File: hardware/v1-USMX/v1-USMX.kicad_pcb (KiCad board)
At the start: 2 copper layers, 91.4 x 48.8 mm, 38 parts, among them IC1 MAX98357AETE+T (L), IC2 MAX98357AETE+T (R), J1 +5v_POWER, J2 Conn_01x04, J3 10118192-0002LF, J4 Serial_Breakout, U1 ESP32-S3-WROOM-1, U2 AZ1084-3.3

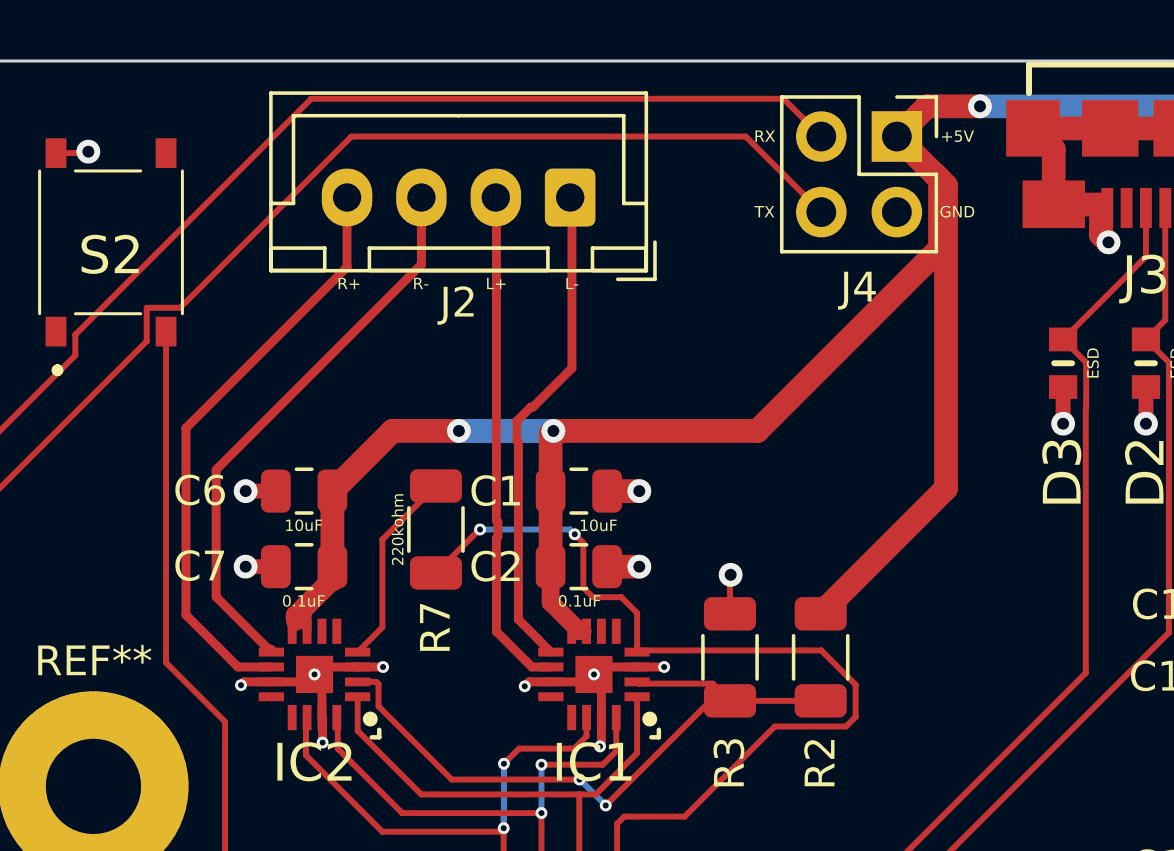
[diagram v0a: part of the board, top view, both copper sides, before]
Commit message: Increased the size of some silk screen
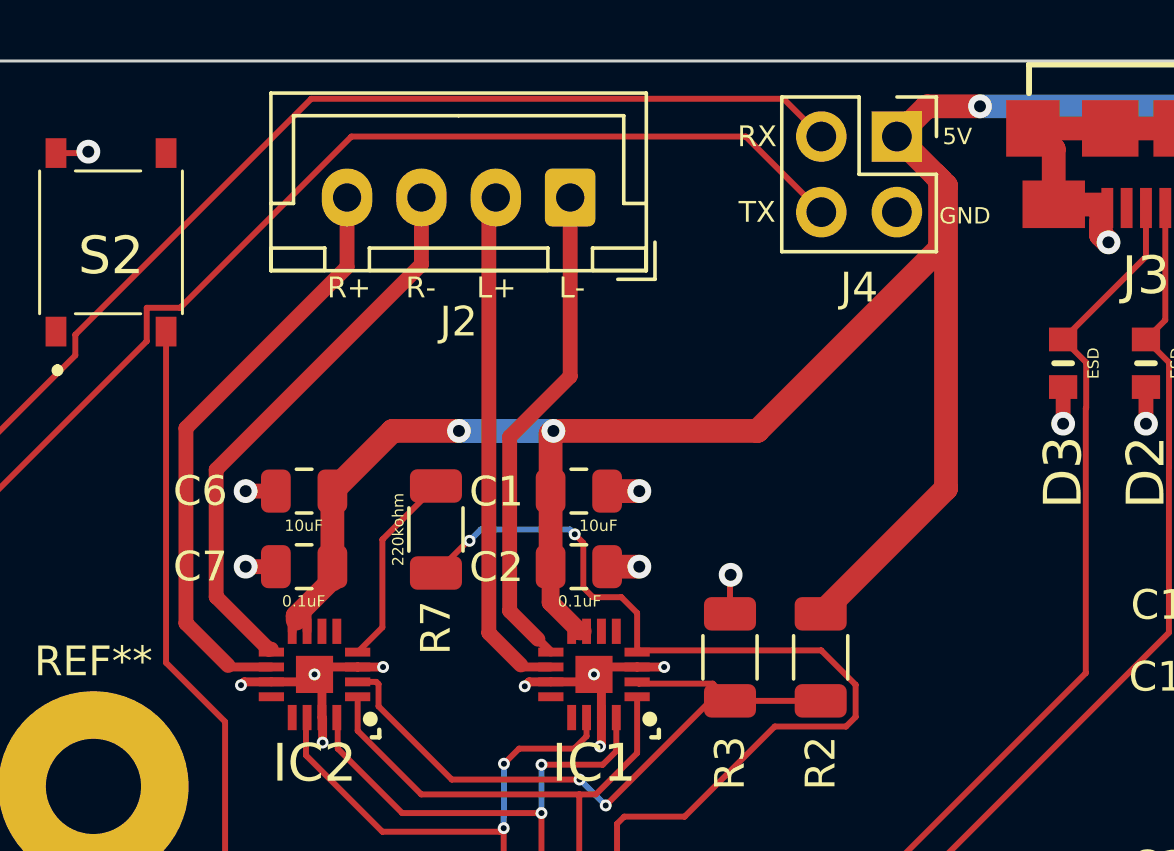
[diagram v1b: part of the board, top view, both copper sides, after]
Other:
- board text added: "5V"
- board text removed: "+5V"

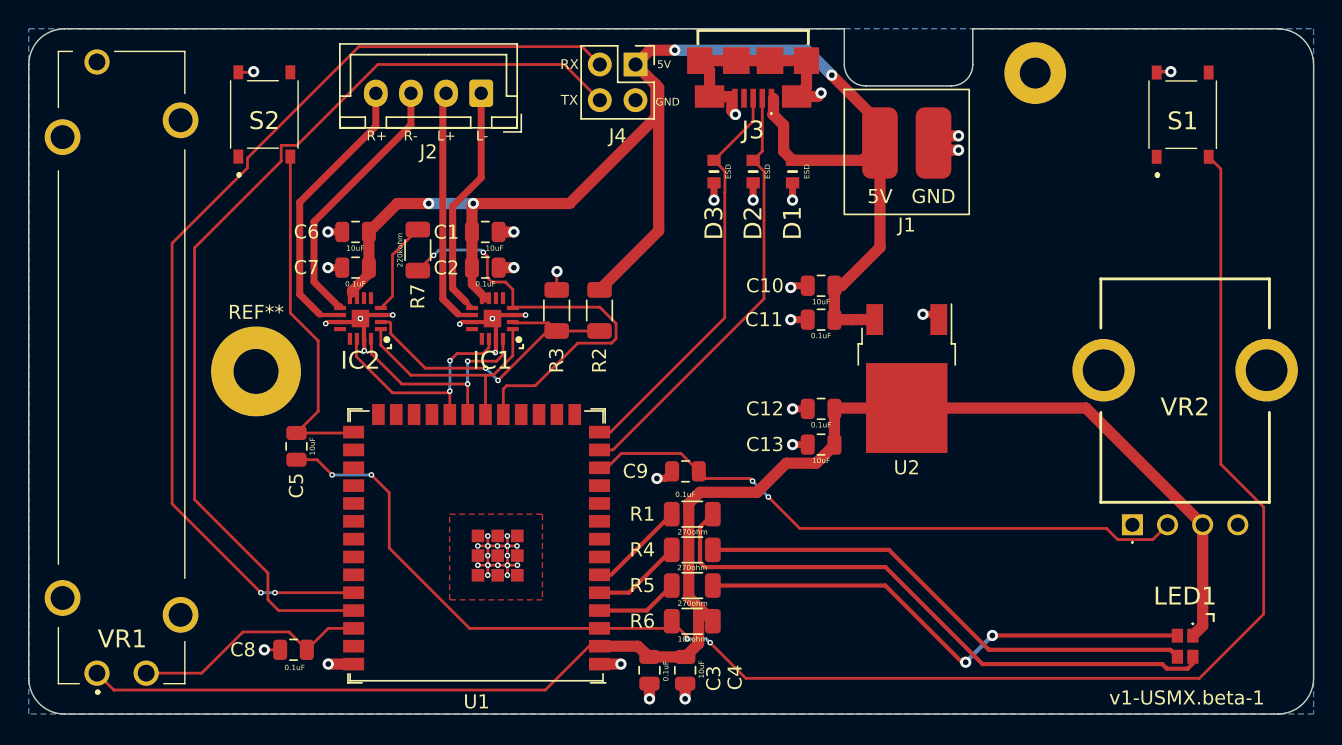
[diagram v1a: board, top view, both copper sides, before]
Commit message: Added ground plane to top, vias at extremeties
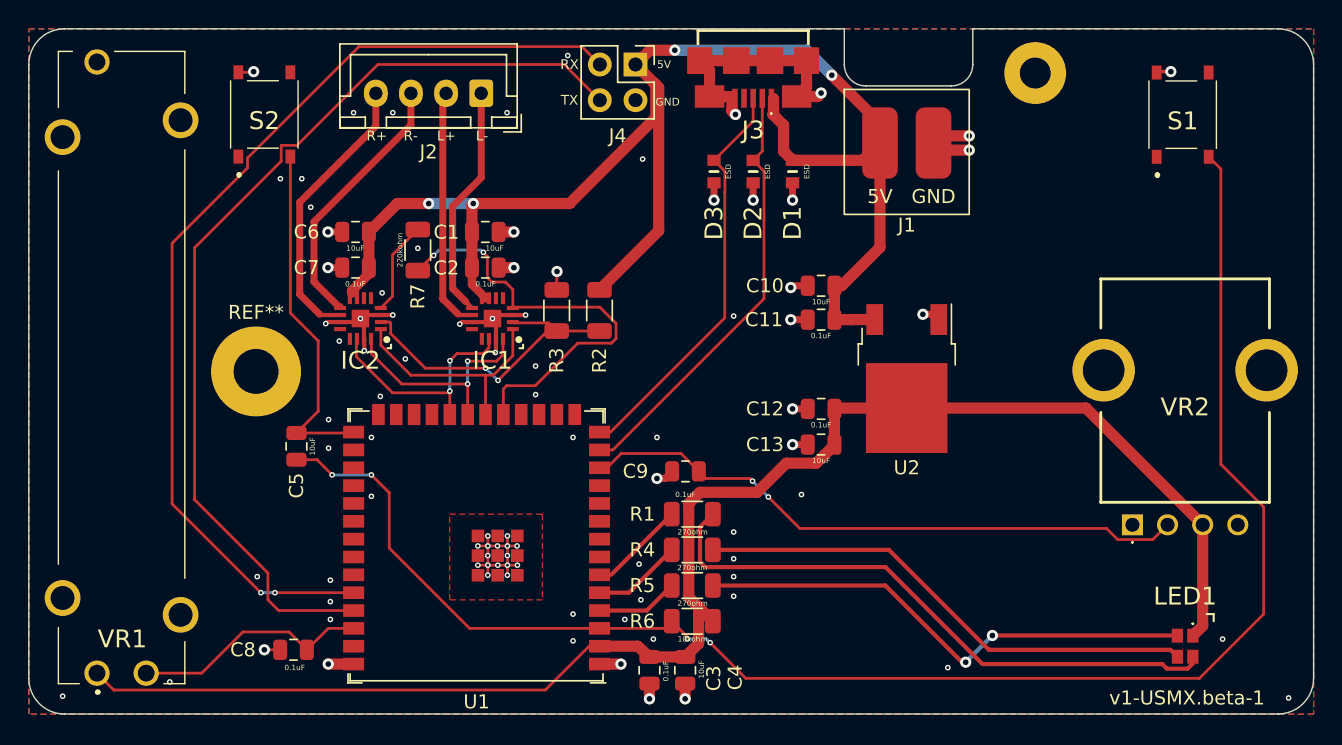
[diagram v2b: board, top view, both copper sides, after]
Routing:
- net GND: track 72.3 -> 73.9 mm, vias 49 -> 91

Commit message: Removed unused screw holes, corrected shape of pads
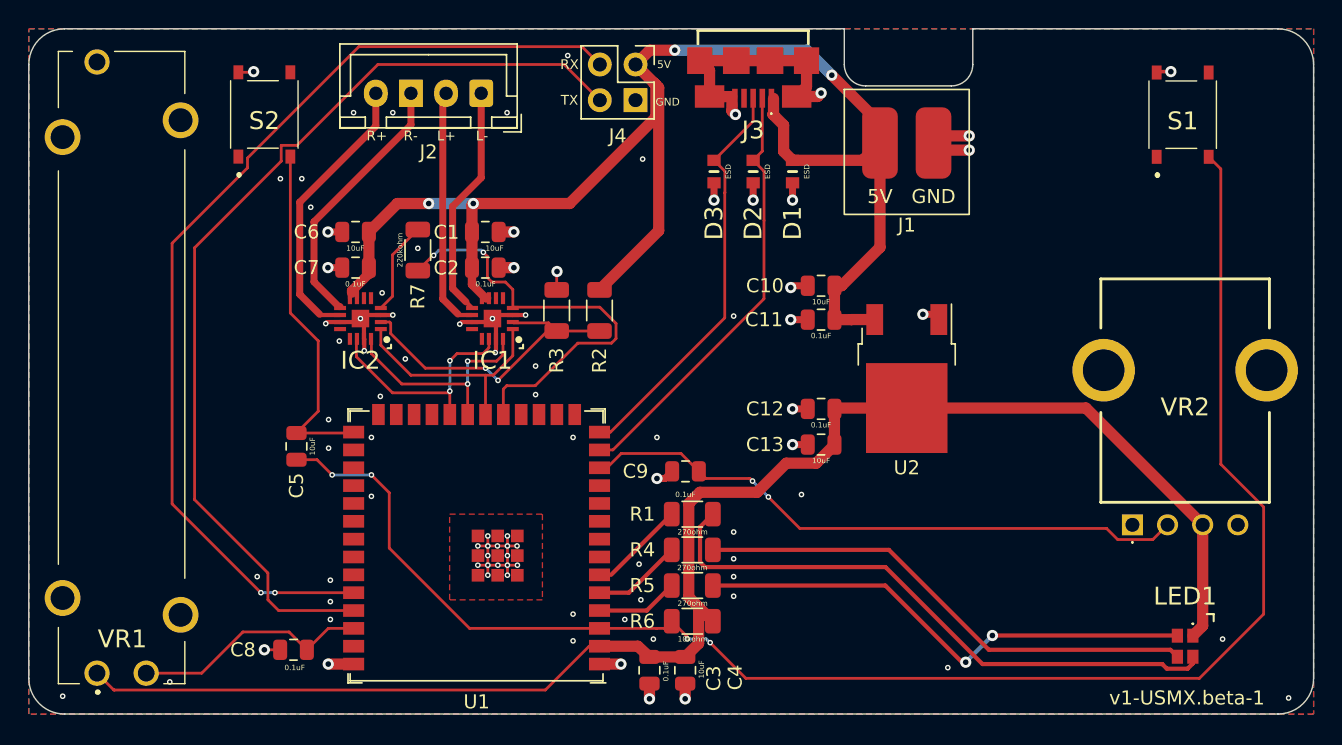
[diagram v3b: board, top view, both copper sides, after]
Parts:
- removed ?: , 
- removed REF**: MountingHole_3.2mm_M3_Pad, MountingHole:MountingHole_3.2mm_M3_Pad
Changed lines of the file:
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@@
     )
-  )
-  (footprint "" locked (layer "F.Cu")
-    (at 170.18 83.4136)
-    (fp_text reference "" (at 0 0) (layer "F.SilkS")
-      (effects (font (size 1.27 1.27) (thickness 0.15)))
-    )
-    (fp_text value "" (at 0 0) (layer "F.SilkS")
-      (effects (font (size 1.27 1.27) (thickness 0.15)))
-    )
-    (pad "1" thru_hole circle locked (at 0 0) (size 4.4 4.4) (drill 2.2) (layers F&B.Cu *.Mask))
   )
   (footprint "my-footprints:PTS526SM08SMTR2LFS" locked (layer "F.Cu")
@@
     (fp_line (start 3.81 3.81) (end -1.27 3.81) (layer "F.Fab") (width 0.1))
     (fp_line (start 0 -1.27) (end 3.81 -1.27) (layer "F.Fab") (width 0.1))
-    (pad "1" thru_hole rect locked (at 0 0 270) (size 1.7 1.7) (drill 1) (layers *.Cu *.Mask)
+    (pad "1" thru_hole oval locked (at 0 0 270) (size 1.7 1.7) (drill 1) (layers *.Cu *.Mask)
       (net 1 "+5V") (pinfunction "Pin_1") (pintype "passive"))
-    (pad "2" thru_hole oval locked (at 2.54 0 270) (size 1.7 1.7) (drill 1) (layers *.Cu *.Mask)
+    (pad "2" thru_hole rect locked (at 2.54 0 270) (size 1.7 1.7) (drill 1) (layers *.Cu *.Mask)
       (net 2 "GND") (pinfunction "Pin_2") (pintype "passive"))
     (pad "3" thru_hole oval locked (at 0 2.54 270) (size 1.7 1.7) (drill 1) (layers *.Cu *.Mask)
@@
     (pad "2" thru_hole oval locked (at 2.5 0 180) (size 1.7 1.95) (drill 0.95) (layers *.Cu *.Mask)
       (net 16 "/LEFT_SPK+") (pinfunction "Pin_2") (pintype "passive"))
-    (pad "3" thru_hole oval locked (at 5 0 180) (size 1.7 1.95) (drill 0.95) (layers *.Cu *.Mask)
+    (pad "3" thru_hole rect locked (at 5 0 180) (size 1.7 1.95) (drill 0.95) (layers *.Cu *.Mask)
       (net 27 "/RIGHT_SPK-") (pinfunction "Pin_3") (pintype "passive"))
     (pad "4" thru_hole oval locked (at 7.5 0 180) (size 1.7 1.95) (drill 0.95) (layers *.Cu *.Mask)
@@
     )
   )
-  (footprint "MountingHole:MountingHole_3.2mm_M3_Pad" locked (layer "F.Cu")
-    (at 114.72472 104.648)
-    (descr "Mounting Hole 3.2mm, M3")
-    (tags "mounting hole 3.2mm m3")
-    (attr exclude_from_pos_files exclude_from_bom)
-    (fp_text reference "REF**" (at 0 -4.2) (layer "F.SilkS")
-      (effects (font (size 1 1) (thickness 0.15)))
-    )
-    (fp_text value "MountingHole_3.2mm_M3_Pad" (at 0 4.2) (layer "F.Fab")
-      (effects (font (size 1 1) (thickness 0.15)))
-    )
-    (fp_text user "${REFERENCE}" (at 0 0) (layer "F.Fab")
-      (effects (font (size 1 1) (thickness 0.15)))
-    )
-    (fp_circle (center 0 0) (end 3.2 0) (layer "Cmts.User") (width 0.15) (fill none))
-    (fp_circle (center 0 0) (end 3.45 0) (layer "F.CrtYd") (width 0.05) (fill none))
-    (pad "1" thru_hole circle locked (at 0 0) (size 6.4 6.4) (drill 3.2) (layers *.Cu *.Mask))
-  )
   (footprint "Capacitor_SMD:C_0805_2012Metric" locked (layer "F.Cu")

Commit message: Moved serial pins to an area that offers easier access with a clamp fixture, even after installation
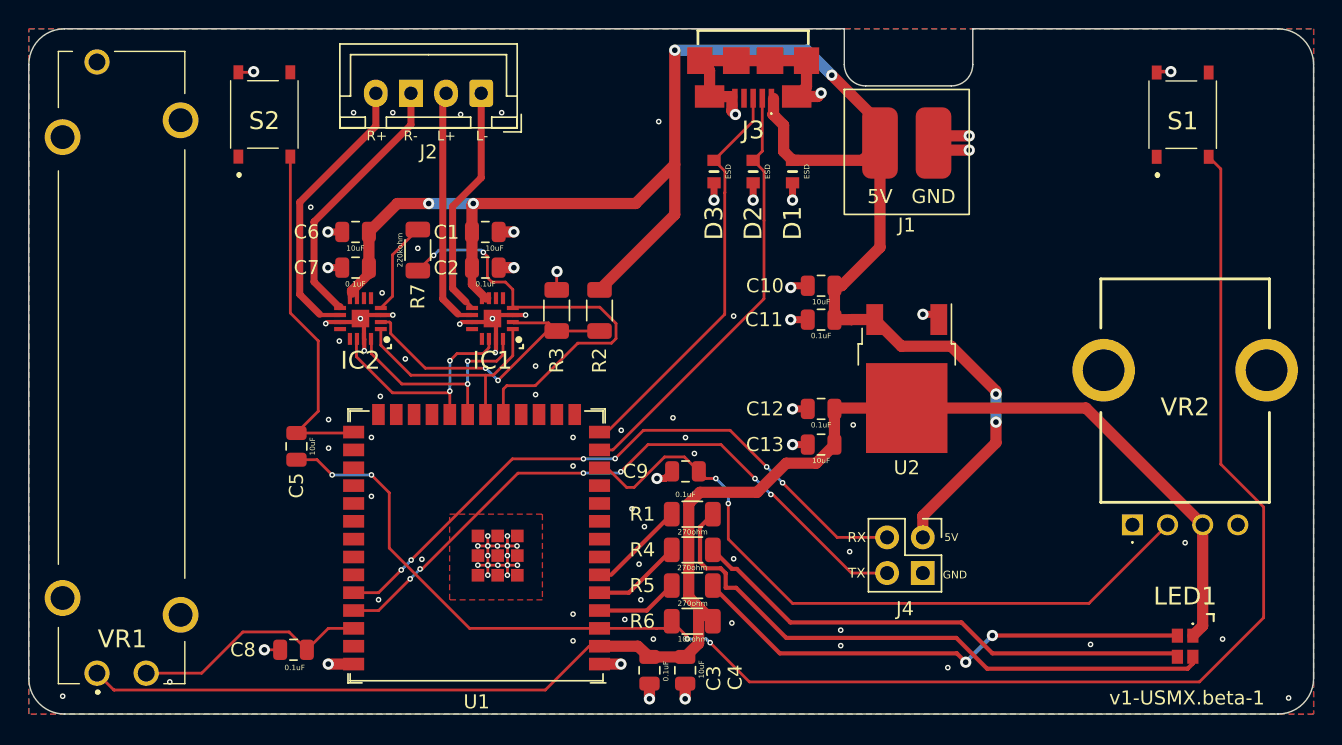
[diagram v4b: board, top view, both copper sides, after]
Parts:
- moved J4 39.4 mm to (162.2, 116.5)
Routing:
- net /U0RXD_TX: track 71.3 -> 45.9 mm, vias 2 -> 6
- net /U0TXD_RX: track 69.6 -> 46.6 mm, vias 0 -> 6
- net +5V: track 108.4 -> 126.8 mm, vias 4 -> 6
- net /V_POT_GPIO08: track 43.8 -> 50.5 mm
- net Net-(LED1-Pad2): track 42.6 -> 43.2 mm
- net GND: vias 91 -> 96

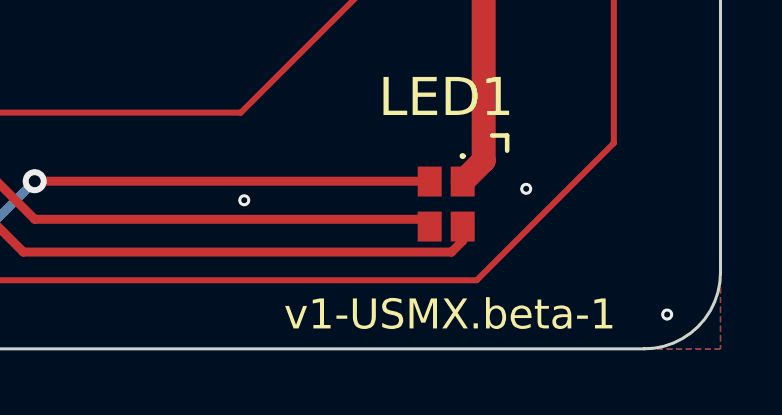
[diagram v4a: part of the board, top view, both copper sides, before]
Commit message: Changed pcb version number
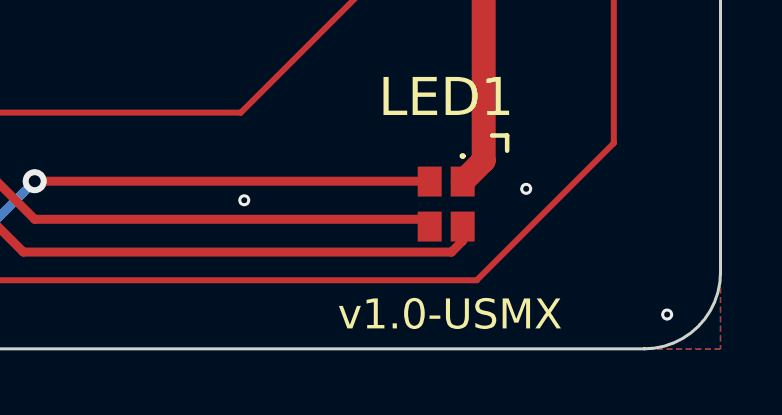
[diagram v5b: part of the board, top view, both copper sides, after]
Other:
- board text added: "v1.0-USMX"
- board text removed: "v1-USMX.beta-1"
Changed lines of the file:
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@@
     (effects (font (size 0.381 0.381) (thickness 0.09525)))
   )
-  (gr_text "v1-USMX.beta-1" (at 180.975 127.889) (layer "F.SilkS")
+  (gr_text "v1.0-USMX" (at 180.975 127.889) (layer "F.SilkS")
     (effects (font (size 1 1) (thickness 0.15)))
   )
